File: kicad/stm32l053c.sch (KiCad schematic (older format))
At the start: 58 parts, among them J1 Water_Level, J2 Motion, J3 Door, J4 Door_Led, J5 AIN3, J6 Pump, J7 BATTERY, P1 SWD, Q1 Q_NMOS_GSD, Q2 Q_PMOS_GSD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

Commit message: Power layout
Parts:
- removed J5: AIN3, Connector_PinHeader_2.54mm:PinHeader_1x02_P2.54mm_Vertical, symbol Connector:Conn_01x02_Female
- removed R14: 620K, Resistor_SMD:R_0805_2012Metric_Pad1.15x1.40mm_HandSolder, symbol stm32l053c-rescue:R
- removed R15: 100K, Resistor_SMD:R_0805_2012Metric_Pad1.15x1.40mm_HandSolder, symbol stm32l053c-rescue:R
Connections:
- net AIN3: now also R8.2, R9.1
- net Earth: now also C12.2, C5.2
- net SENSOR_PWR: now also U2.39 (PB3); no longer U2.14 (PA4)
- net WATER_LEVEL: now also U2.38 (PA15); no longer U2.11 (PA1)
- net WATER_TEMP: now also U3.6 (AIN2); no longer U2.10 (PAO)
- removed net AIN2: R8.2, R9.1, U3.6 (AIN2)
- no-connect marks 18 -> 19
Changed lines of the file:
@@
 	1    0    0    -1
 $EndComp
-Text Label 1900 5125 0    60   ~ 0
-AIN2
 $Comp
 L stm32l053c-rescue:R R9
@@
 Wire Wire Line
 	1300 6425 1375 6425
-Wire Wire Line
-	1900 5125 2150 5125
 Wire Wire Line
 	9525 1675 9525 1800
@@
 	2200 1625 2200 1675
 Text Label 1950 1625 0    60   ~ 0
-AIN2
+AIN3
 Connection ~ 2200 1625
 Text Label 1850 4525 2    60   ~ 0
@@
 NoConn ~ 4350 6525
 NoConn ~ 4350 6425
-NoConn ~ 10625 3000
+NoConn ~ 8675 3100
 NoConn ~ 10625 3500
 Text GLabel 1925 3375 2    60   Input ~ 0
@@
 	1    0    0    -1
 $EndComp
-Text GLabel 8675 2700 0    60   Input ~ 0
+Text GLabel 1800 5125 0    60   Input ~ 0
 WATER_TEMP
 Text GLabel 10625 4800 2    60   Input ~ 0
@@
 	0    1    1    0
 $EndComp
-Text GLabel 8675 3100 0    60   Input ~ 0
+Text GLabel 10625 3000 2    60   Input ~ 0
 SENSOR_PWR
 Text GLabel 5800 2025 0    60   Input ~ 0
@@
 	5875 1050 6050 1050
 Connection ~ 6050 1050
-Text GLabel 8675 2800 0    60   Input ~ 0
+Text GLabel 8675 4200 0    60   Input ~ 0
 WATER_LEVEL
 $Comp
@@
 PUMP
 Connection ~ 2850 4225
-$Comp
-L stm32l053c-rescue:R R15
-U 1 1 5C27DDBD
-P 1650 5375
-F 0 "R15" V 1730 5375 50  0000 C CNN
-F 1 "100K" V 1650 5375 50  0000 C CNN
-F 2 "Resistor_SMD:R_0805_2012Metric_Pad1.15x1.40mm_HandSolder" V 1580 5375 50  0001 C CNN
-F 3 "" H 1650 5375 50  0001 C CNN
-	1    1650 5375
-	1    0    0    -1
-$EndComp
-$Comp
-L stm32l053c-rescue:R R14
-U 1 1 5C27DDC4
-P 1500 5225
-F 0 "R14" V 1580 5225 50  0000 C CNN
-F 1 "620K" V 1500 5225 50  0000 C CNN
-F 2 "Resistor_SMD:R_0805_2012Metric_Pad1.15x1.40mm_HandSolder" V 1430 5225 50  0001 C CNN
-F 3 "" H 1500 5225 50  0001 C CNN
-	1    1500 5225
-	0    1    1    0
-$EndComp
-$Comp
-L power:Earth #PWR036
-U 1 1 5C27DDCB
-P 1450 5525
-F 0 "#PWR036" H 1450 5275 50  0001 C CNN
-F 1 "Earth" H 1450 5375 50  0001 C CNN
-F 2 "" H 1450 5525 50  0000 C CNN
-F 3 "" H 1450 5525 50  0000 C CNN
-	1    1450 5525
-	-1   0    0    -1
-$EndComp
-$Comp
-L Connector:Conn_01x02_Female J5
-U 1 1 5C280156
-P 1150 5325
-F 0 "J5" H 1044 5000 50  0000 C CNN
-F 1 "AIN3" H 1044 5091 50  0000 C CNN
-F 2 "Connector_PinHeader_2.54mm:PinHeader_1x02_P2.54mm_Vertical" H 1150 5325 50  0001 C CNN
-F 3 "~" H 1150 5325 50  0001 C CNN
-	1    1150 5325
-	-1   0    0    1
-$EndComp
-Wire Wire Line
-	1350 5325 1350 5525
-Wire Wire Line
-	1350 5525 1450 5525
-Wire Wire Line
-	1650 5525 1450 5525
-Connection ~ 1450 5525
-Wire Wire Line
-	1650 5225 2150 5225
-Connection ~ 1650 5225
 Text GLabel 6650 4550 2    60   Input ~ 0
 DOOR_LED
@@
 NoConn ~ 8675 3600
 NoConn ~ 8675 3700
-NoConn ~ 8675 4200
+NoConn ~ 8675 2800
 $Comp
 L Device:LED_CRGB D2
@@
 	3525 1475 3450 1475
 Connection ~ 3450 1475
+Wire Wire Line
+	3450 1925 3825 1925
+Connection ~ 3450 1925
+Wire Wire Line
+	1900 5225 2150 5225
+Wire Wire Line
+	1800 5125 2150 5125
+NoConn ~ 8675 2700
 $EndSCHEMATC

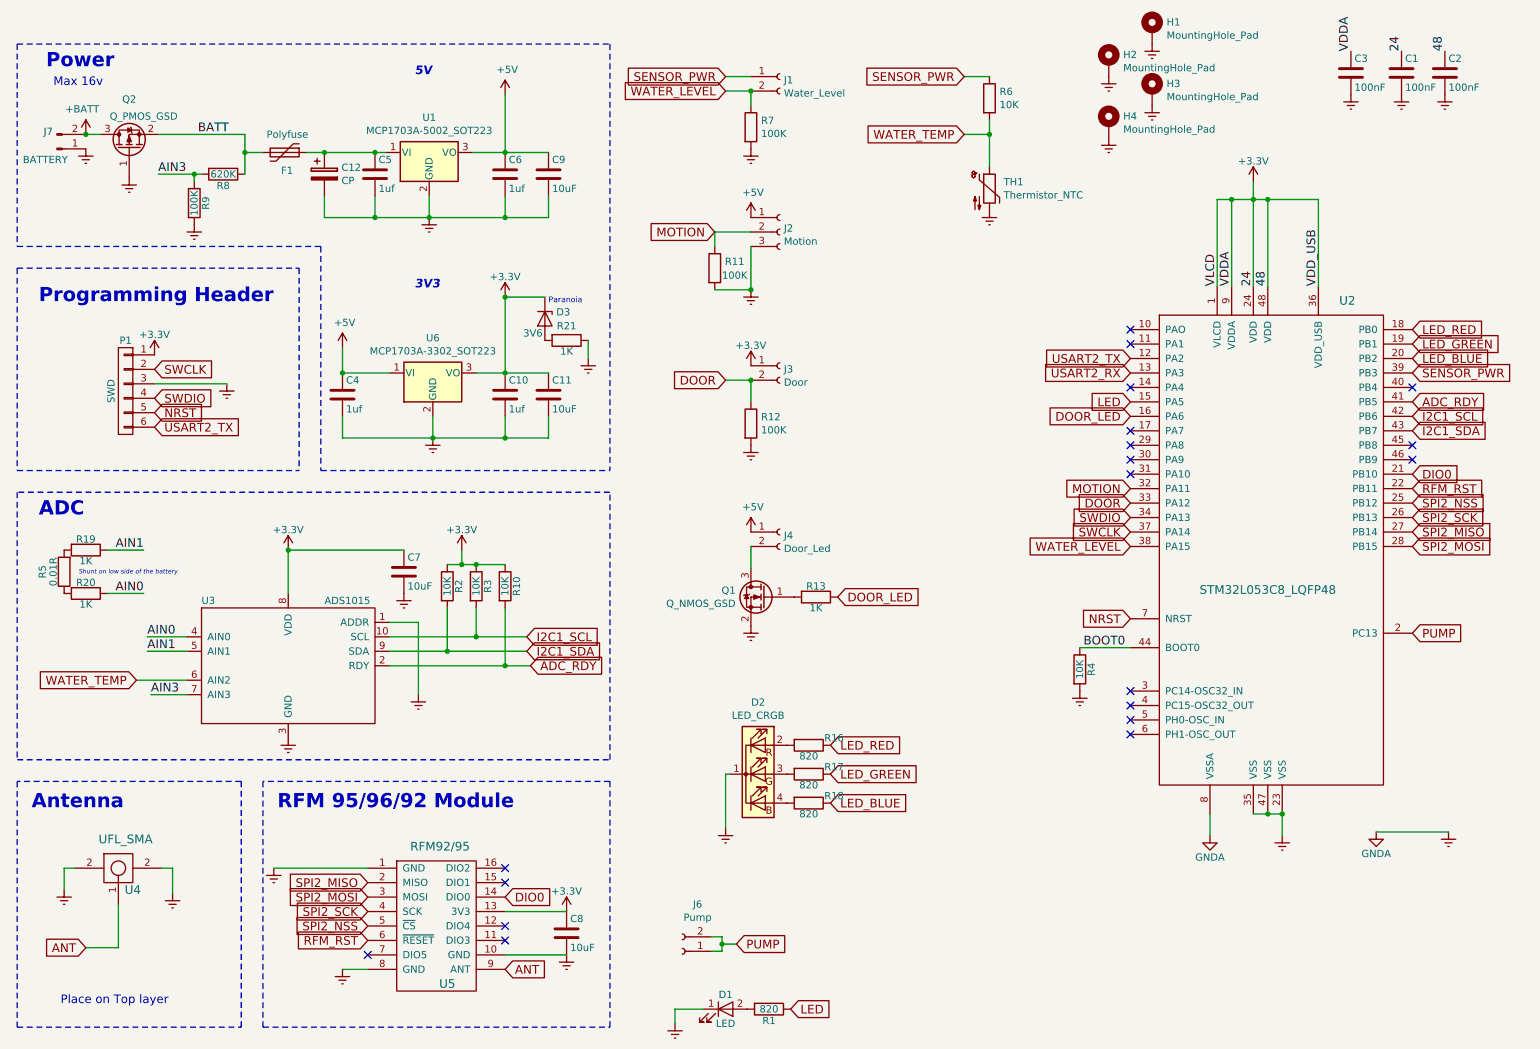
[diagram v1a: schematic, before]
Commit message: Changed the overvoltage protection
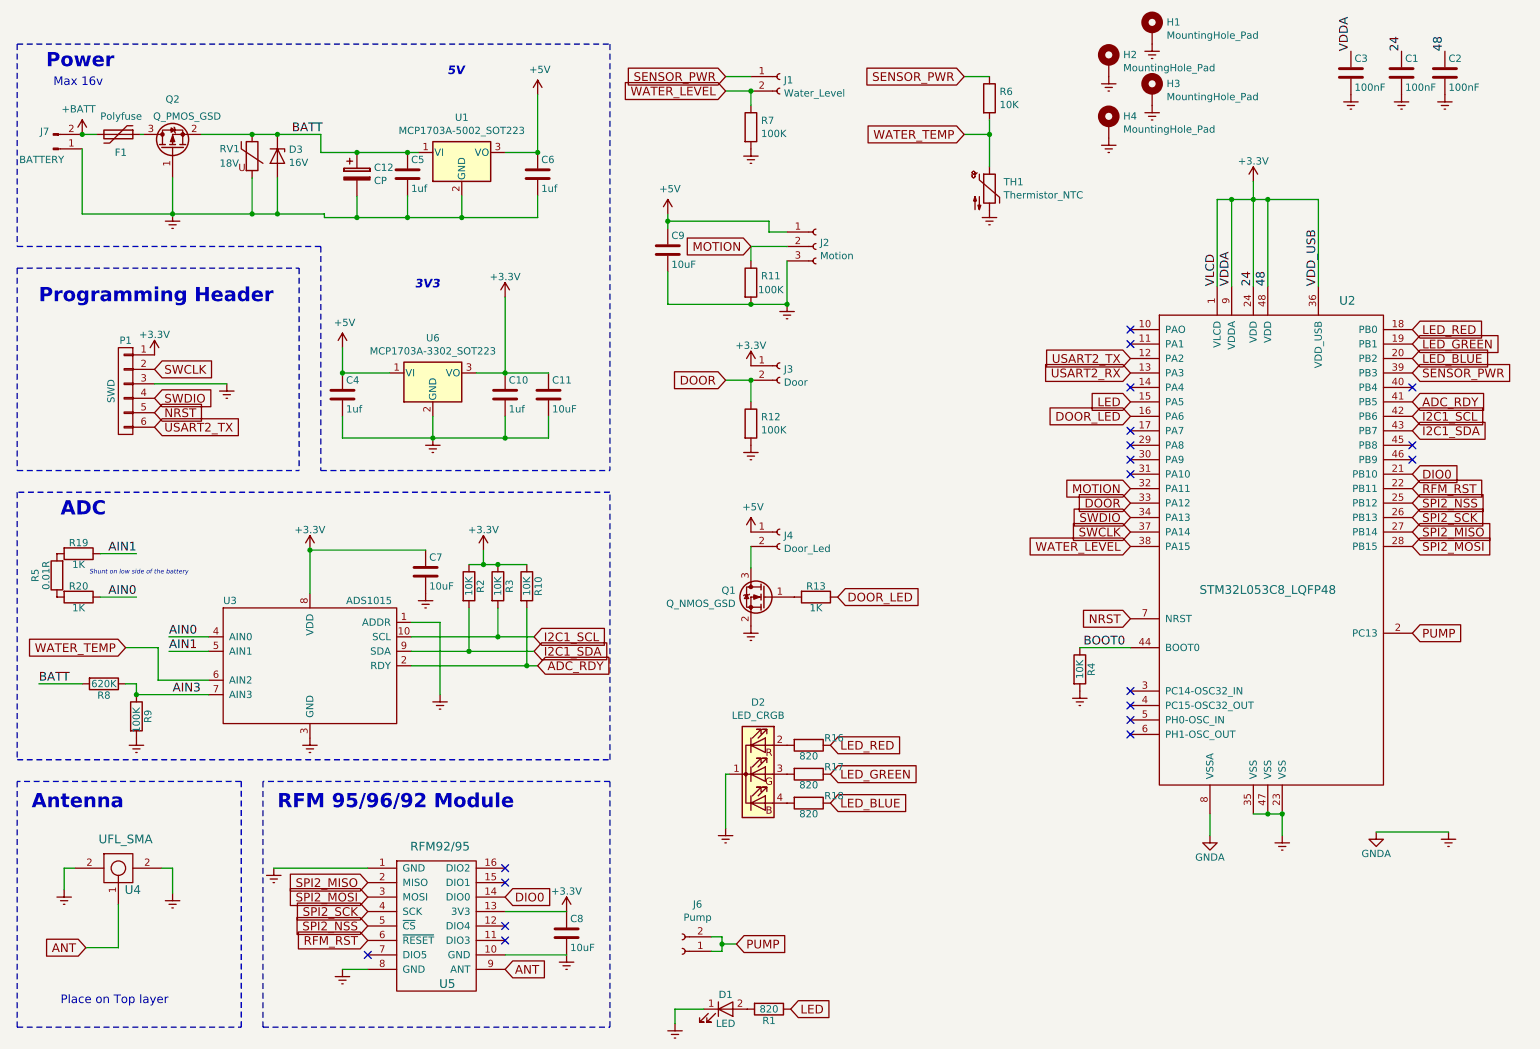
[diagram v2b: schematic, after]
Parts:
- removed R21: 1K, Resistor_SMD:R_0603_1608Metric_Pad1.05x0.95mm_HandSolder, symbol Device:R
- added RV1: 18V, Varistor:RV_Disc_D7mm_W5.4mm_P5mm, symbol Device:Varistor
- D3: value 3V6 -> 16V
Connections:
- net +3V3: no longer D3.1 (K)
- net +BATT: now also F1.2; no longer Q2.3 (D)
- net AIN3: now also R8.1; no longer R8.2
- net BATT: now also C12.1, C5.1, D3.1 (K), R8.2, U1.1 (VI), RV1.1; no longer F1.2, R8.1
- net Earth: now also D3.2 (A), RV1.2
- new net: F1.1, Q2.3 (D)
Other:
- note removed: "Paranoia"
- moved on the sheet: C12, C5, C6, C7, C9, F1, J2, J7, Q2, R10, R11, R19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

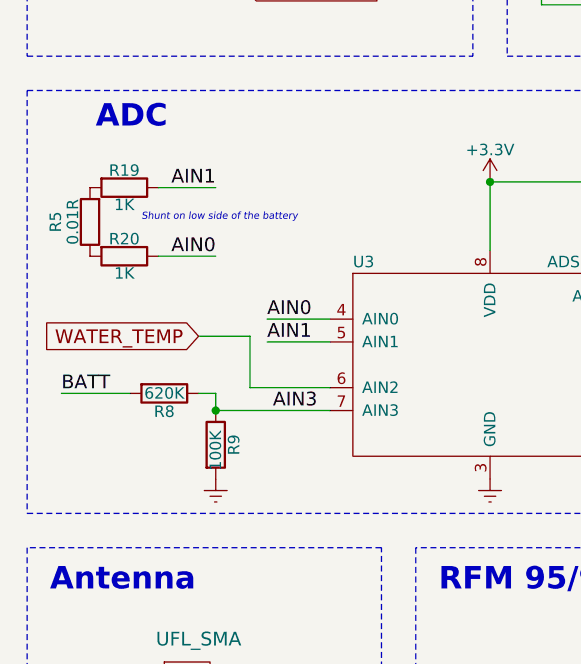
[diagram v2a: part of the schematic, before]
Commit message: Reassign ADC pins
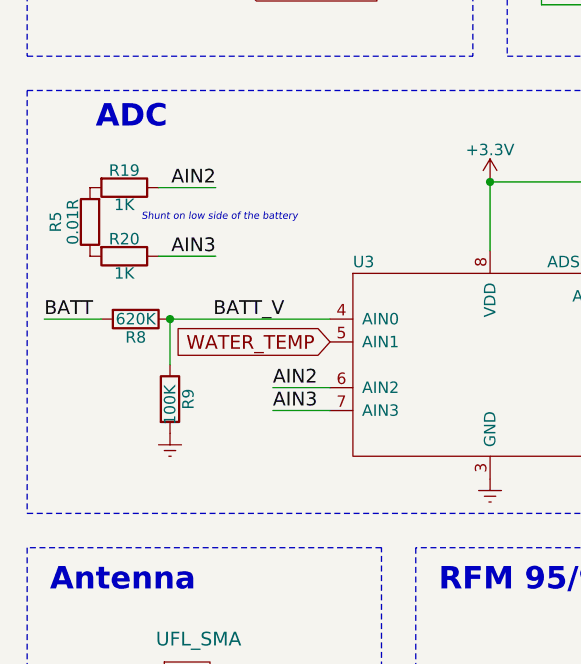
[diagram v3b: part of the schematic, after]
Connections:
- net AIN3: now also R20.1; no longer R8.1, R9.1
- net WATER_TEMP: now also U3.5 (AIN1); no longer U3.6 (AIN2)
- net AIN0 renamed BATT_V
- net BATT_V: now also R8.1, R9.1; no longer R20.1
- net AIN1 renamed AIN2
- net AIN2: now also U3.6 (AIN2); no longer U3.5 (AIN1)
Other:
- moved on the sheet: R8, R9
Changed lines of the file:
@@
 L stm32l053c-rescue:R R9
 U 1 1 59356DA1
-P 1800 5375
-F 0 "R9" V 1880 5375 50  0000 C CNN
-F 1 "100K" V 1800 5350 50  0000 C CNN
-F 2 "Resistor_SMD:R_0805_2012Metric_Pad1.15x1.40mm_HandSolder" V 1730 5375 50  0001 C CNN
-F 3 "" H 1800 5375 50  0001 C CNN
-	1    1800 5375
+P 1600 5175
+F 0 "R9" V 1680 5175 50  0000 C CNN
+F 1 "100K" V 1600 5150 50  0000 C CNN
+F 2 "Resistor_SMD:R_0805_2012Metric_Pad1.15x1.40mm_HandSolder" V 1530 5175 50  0001 C CNN
+F 3 "" H 1600 5175 50  0001 C CNN
+	1    1600 5175
 	1    0    0    -1
 $EndComp
@@
 L stm32l053c-rescue:R R8
 U 1 1 59356E2E
-P 1575 5150
-F 0 "R8" V 1655 5150 50  0000 C CNN
-F 1 "620K" V 1575 5150 50  0000 C CNN
-F 2 "Resistor_SMD:R_0805_2012Metric_Pad1.15x1.40mm_HandSolder" V 1505 5150 50  0001 C CNN
-F 3 "" H 1575 5150 50  0001 C CNN
-	1    1575 5150
+P 1450 4825
+F 0 "R8" V 1530 4825 50  0000 C CNN
+F 1 "620K" V 1450 4825 50  0000 C CNN
+F 2 "Resistor_SMD:R_0805_2012Metric_Pad1.15x1.40mm_HandSolder" V 1380 4825 50  0001 C CNN
+F 3 "" H 1450 4825 50  0001 C CNN
+	1    1450 4825
 	0    1    1    0
 $EndComp
@@
 L power:Earth #PWR030
 U 1 1 59357323
-P 1800 5525
-F 0 "#PWR030" H 1800 5275 50  0001 C CNN
-F 1 "Earth" H 1800 5375 50  0001 C CNN
-F 2 "" H 1800 5525 50  0000 C CNN
-F 3 "" H 1800 5525 50  0000 C CNN
-	1    1800 5525
+P 1600 5325
+F 0 "#PWR030" H 1600 5075 50  0001 C CNN
+F 1 "Earth" H 1600 5175 50  0001 C CNN
+F 2 "" H 1600 5325 50  0000 C CNN
+F 3 "" H 1600 5325 50  0000 C CNN
+	1    1600 5325
 	-1   0    0    -1
 $EndComp
@@
 	1    0    0    -1
 $EndComp
-Text Label 2025 4925 0    60   ~ 0
-AIN1
-Text Label 2025 4825 0    60   ~ 0
-AIN0
+Text Label 2100 4825 2    60   ~ 0
+BATT_V
 Text Label 2050 5225 0    60   ~ 0
 AIN3
@@
 Wire Wire Line
 	8325 4900 8675 4900
-Wire Wire Line
-	2025 4825 2300 4825
-Wire Wire Line
-	2025 4925 2300 4925
 Wire Wire Line
 	2050 6600 2050 6425
@@
 Connection ~ 4500 5025
 Connection ~ 4300 4325
-Text Label 1800 4550 2    60   ~ 0
-AIN0
-Text Label 1800 4250 2    60   ~ 0
-AIN1
 Text Label 2875 1350 0    60   ~ 0
 BATT
@@
 	1    0    0    -1
 $EndComp
-Text GLabel 1725 4900 0    60   Input ~ 0
+Text GLabel 2300 4925 0    60   Input ~ 0
 WATER_TEMP
 Text GLabel 10625 4800 2    60   Input ~ 0
@@
 	3675 1925 4050 1925
 Connection ~ 3675 1925
-Wire Wire Line
-	1950 5125 2300 5125
 NoConn ~ 8675 2700
 Wire Wire Line
@@
 	0    1    1    0
 $EndComp
-Text Label 1125 5150 0    60   ~ 0
+Text Label 1050 4825 0    60   ~ 0
 BATT
-Wire Wire Line
-	1725 4900 1950 4900
-Wire Wire Line
-	1950 4900 1950 5125
-Wire Wire Line
-	1800 5150 1800 5225
-Wire Wire Line
-	1800 5225 2300 5225
-Wire Wire Line
-	1725 5150 1800 5150
-Wire Wire Line
-	1125 5150 1425 5150
-Connection ~ 1800 5225
 $Comp
 L Device:Varistor RV1
@@
 Connection ~ 2775 1900
 Connection ~ 3325 1925
+Text Label 1800 4250 2    60   ~ 0
+AIN2
+Text Label 1800 4550 2    60   ~ 0
+AIN3
+Wire Wire Line
+	2050 5225 2300 5225
+Text Label 2050 5125 0    60   ~ 0
+AIN2
+Wire Wire Line
+	2300 5125 2050 5125
+Wire Wire Line
+	1300 4825 1050 4825
+Wire Wire Line
+	1600 4825 1600 5025
+Wire Wire Line
+	1600 4825 2300 4825
+Connection ~ 1600 4825
 $EndSCHEMATC

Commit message: All connected
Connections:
- net DOOR_LED: now also U2.2 (PC13); no longer U2.16 (PA6)
- net PUMP: now also U2.16 (PA6); no longer U2.2 (PC13)
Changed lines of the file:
@@
 Text GLabel 2300 4925 0    60   Input ~ 0
 WATER_TEMP
-Text GLabel 10625 4800 2    60   Input ~ 0
+Text GLabel 8675 3300 0    60   Input ~ 0
 PUMP
 Text GLabel 8675 3900 0    60   Input ~ 0
@@
 Wire Wire Line
 	5875 950  6050 950
-Text GLabel 8675 3300 0    60   Input ~ 0
+Text GLabel 10625 4800 2    60   Input ~ 0
 DOOR_LED
 $Comp
